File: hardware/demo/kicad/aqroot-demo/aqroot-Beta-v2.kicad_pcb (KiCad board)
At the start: 6 copper layers, 72 x 148 mm, 311 parts, among them J1 FH69-50S-0.5SH, J2 Molex_5025700893, J3 USB_C_Receptacle_USB2.0_16P, J4 JST-PH-2 BATTERY, J5 COMMUNITY_PORT_1x24, J6 JST-PH-2 SPEAKER, J7 BM02B-ACHSS-GAN-ETF, J8 QWIIC_STEMMA_QT, Q1 AO3400A, Q10 2N7002, Q2 NTMD4820N, Q3 NTMD4820N, Q4 BSS138, Q5 AO3401A, Q6 BSS138, Q7 BSS138, Q8 BSS138, Q9 BSS138, SW1 BOOT, SW2 UP, SW3 DOWN, SW4 LEFT, SW5 RIGHT, SW6 A_SELECT, SW7 B_BACK, SW9 SW_SPDT, U1 ESP32-S3-WROOM-1, U10 USBLC6-2SC6, U11 BQ25185, U12 TPS63020, U13 TPS61023, U14 MAX17048, U16 TCA4307DGKR, U17 TPS61169DCKR, U18 LTC4368-1, U19 TLV7032, U2 PCAL9535APW, U20 TPS22950C, U21 TPS61023, U22 TPS22950C, U3 PCAL9535APW, U4 BMI270, U5 MAX98357A, U6 TSOP38238, U7 E07-400M10S, U8 E22-900M22S, U9 ST25R3916-AQET, Y1 27.12MHz 10pF 3225-4P

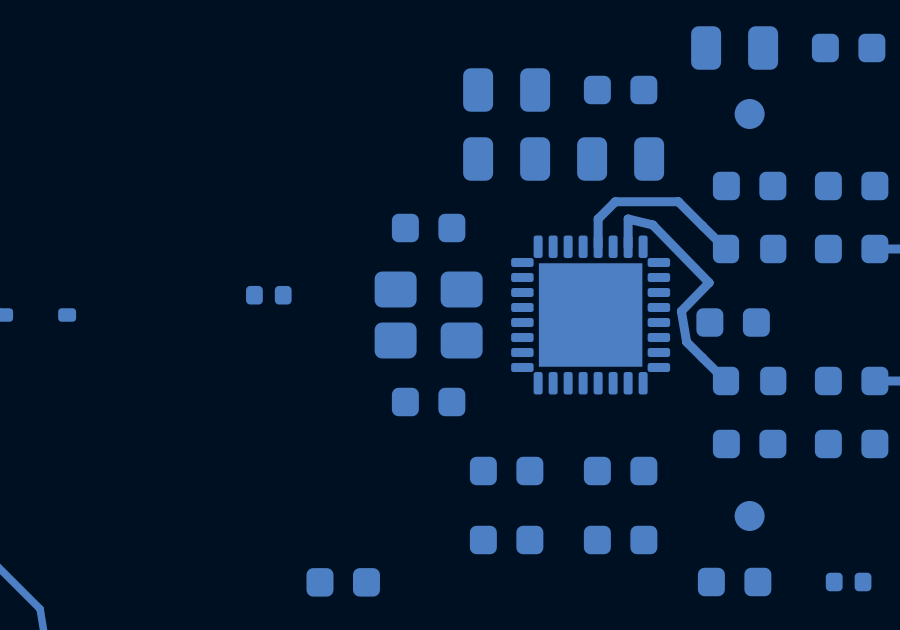
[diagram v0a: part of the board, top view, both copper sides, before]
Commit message: demo: route NFC crystal pair
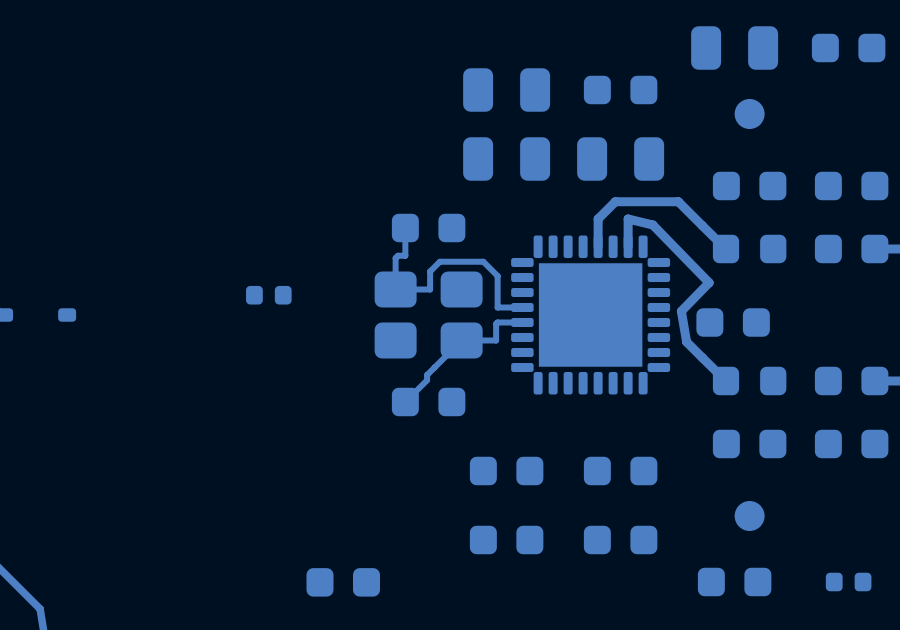
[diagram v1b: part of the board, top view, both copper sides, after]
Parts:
- moved C79 5.80 mm to (28.6, 32.9)
- moved C80 5.80 mm to (28.6, 27.1)
- turned Y1 to 180 degrees
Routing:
- net /04_SPI_B_RADIOS_NFC/NFC_XIN: track 0.00 -> 8.54 mm
- net /04_SPI_B_RADIOS_NFC/NFC_XOUT: track 0.00 -> 5.42 mm
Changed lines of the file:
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@@
 	(footprint "Capacitor_SMD:C_0603_1608Metric"
 		(layer "B.Cu")
-		(at 28.6 32.9)
+		(at 28.6 27.1)
 		(descr "Unpolarized capacitor")
 		(tags "capacitor")
@@
 	(footprint "Capacitor_SMD:C_0603_1608Metric"
 		(layer "B.Cu")
-		(at 28.6 27.1)
+		(at 28.6 32.9)
 		(descr "Unpolarized capacitor")
 		(tags "capacitor")
@@
 	(footprint "Crystal:Crystal_SMD_3225-4Pin_3.2x2.5mm"
 		(layer "B.Cu")
-		(at 28.6 30)
+		(at 28.6 30 180)
 		(descr "Four pin crystal, GND on pins 2 and 4")
 		(property "Reference" "Y1"
-			(at 0 2.45 180)
+			(at 0 2.45 0)
 			(layer "B.SilkS")
 			(hide yes)
@@
 		)
 		(property "Value" "27.12MHz 10pF 3225-4P"
-			(at 0 -2.45 180)
+			(at 0 -2.45 0)
 			(layer "B.Fab")
 			(hide yes)
@@
 		)
 		(property "Datasheet" ""
-			(at 0 0 180)
+			(at 0 0 0)
 			(layer "B.Fab")
 			(hide yes)
@@
 		)
 		(property "Description" ""
-			(at 0 0 180)
+			(at 0 0 0)
 			(layer "B.Fab")
 			(hide yes)
@@
 		)
 		(property "KiLib_Generator" "crystal_resonator_oscillator"
-			(at 0 0 180)
+			(at 0 0 0)
 			(layer "B.SilkS")
 			(hide yes)
@@
 		(duplicate_pad_numbers_are_jumpers no)
 		(fp_line
-			(start -2.06 -1.71)
-			(end 2.06 -1.71)
+			(start -2.06 1.71)
+			(end -2.06 -1.71)
 			(stroke
 				(width 0.12)
@@
 		)
 		(fp_line
-			(start -2.06 1.71)
-			(end -2.06 -1.71)
+			(start -2.06 -1.71)
+			(end 2.06 -1.71)
 			(stroke
 				(width 0.12)
@@
 		)
 		(fp_text user "${REFERENCE}"
-			(at 0 0 180)
+			(at 0 0 0)
 			(layer "B.Fab")
 			(effects
@@
 		)
 		(pad "1" smd roundrect
-			(at -1.1 -0.85)
+			(at -1.1 -0.85 180)
 			(size 1.4 1.2)
 			(layers "B.Cu" "B.Mask" "B.Paste")
@@
 		)
 		(pad "2" smd roundrect
-			(at 1.1 -0.85)
+			(at 1.1 -0.85 180)
 			(size 1.4 1.2)
 			(layers "B.Cu" "B.Mask" "B.Paste")
@@
 		)
 		(pad "3" smd roundrect
-			(at 1.1 0.85)
+			(at 1.1 0.85 180)
 			(size 1.4 1.2)
 			(layers "B.Cu" "B.Mask" "B.Paste")
@@
 		)
 		(pad "4" smd roundrect
-			(at -1.1 0.85)
+			(at -1.1 0.85 180)
 			(size 1.4 1.2)
 			(layers "B.Cu" "B.Mask" "B.Paste")
@@
 	)
 	(segment
+		(start 30.9 30.25)
+		(end 30.85 30.3)
+		(width 0.2)
+		(layer "B.Cu")
+		(net "/04_SPI_B_RADIOS_NFC/NFC_XOUT")
+	)
+	(segment
+		(start 31.725 30.25)
+		(end 30.9 30.25)
+		(width 0.2)
+		(layer "B.Cu")
+		(net "/04_SPI_B_RADIOS_NFC/NFC_XOUT")
+	)
+	(segment
+		(start 27.825 32.9)
+		(end 28.55 32.175)
+		(width 0.2)
+		(layer "B.Cu")
+		(net "/04_SPI_B_RADIOS_NFC/NFC_XOUT")
+	)
+	(segment
+		(start 28.55 32)
+		(end 28.55 32.175)
+		(width 0.2)
+		(layer "B.Cu")
+		(net "/04_SPI_B_RADIOS_NFC/NFC_XOUT")
+	)
+	(segment
+		(start 29.7 30.85)
+		(end 28.8 31.75)
+		(width 0.2)
+		(layer "B.Cu")
+		(net "/04_SPI_B_RADIOS_NFC/NFC_XOUT")
+	)
+	(segment
+		(start 28.8 31.75)
+		(end 28.55 32)
+		(width 0.2)
+		(layer "B.Cu")
+		(net "/04_SPI_B_RADIOS_NFC/NFC_XOUT")
+	)
+	(segment
+		(start 30.85 30.3)
+		(end 30.85 30.85)
+		(width 0.2)
+		(layer "B.Cu")
+		(net "/04_SPI_B_RADIOS_NFC/NFC_XOUT")
+	)
+	(segment
+		(start 29.7 30.85)
+		(end 30.85 30.85)
+		(width 0.2)
+		(layer "B.Cu")
+		(net "/04_SPI_B_RADIOS_NFC/NFC_XOUT")
+	)
+	(segment
+		(start 27.5 29.15)
+		(end 27.5 28.1)
+		(width 0.2)
+		(layer "B.Cu")
+		(net "/04_SPI_B_RADIOS_NFC/NFC_XIN")
+	)
+	(segment
+		(start 30.9 29.75)
+		(end 30.9 28.7)
+		(width 0.2)
+		(layer "B.Cu")
+		(net "/04_SPI_B_RADIOS_NFC/NFC_XIN")
+	)
+	(segment
+		(start 27.5 29.15)
+		(end 28.65 29.15)
+		(width 0.2)
+		(layer "B.Cu")
+		(net "/04_SPI_B_RADIOS_NFC/NFC_XIN")
+	)
+	(segment
+		(start 30.425 28.225)
+		(end 28.975 28.225)
+		(width 0.2)
+		(layer "B.Cu")
+		(net "/04_SPI_B_RADIOS_NFC/NFC_XIN")
+	)
+	(segment
+		(start 28.975 28.225)
+		(end 28.65 28.55)
+		(width 0.2)
+		(layer "B.Cu")
+		(net "/04_SPI_B_RADIOS_NFC/NFC_XIN")
+	)
+	(segment
+		(start 31.725 29.75)
+		(end 30.9 29.75)
+		(width 0.2)
+		(layer "B.Cu")
+		(net "/04_SPI_B_RADIOS_NFC/NFC_XIN")
+	)
+	(segment
+		(start 27.5 28.1)
+		(end 27.575 28.025)
+		(width 0.2)
+		(layer "B.Cu")
+		(net "/04_SPI_B_RADIOS_NFC/NFC_XIN")
+	)
+	(segment
+		(start 30.9 28.7)
+		(end 30.425 28.225)
+		(width 0.2)
+		(layer "B.Cu")
+		(net "/04_SPI_B_RADIOS_NFC/NFC_XIN")
+	)
+	(segment
+		(start 27.575 28.025)
+		(end 27.825 28.025)
+		(width 0.2)
+		(layer "B.Cu")
+		(net "/04_SPI_B_RADIOS_NFC/NFC_XIN")
+	)
+	(segment
+		(start 27.825 27.1)
+		(end 27.825 28.025)
+		(width 0.2)
+		(layer "B.Cu")
+		(net "/04_SPI_B_RADIOS_NFC/NFC_XIN")
+	)
+	(segment
+		(start 28.65 28.55)
+		(end 28.65 29.15)
+		(width 0.2)
+		(layer "B.Cu")
+		(net "/04_SPI_B_RADIOS_NFC/NFC_XIN")
+	)
+	(segment

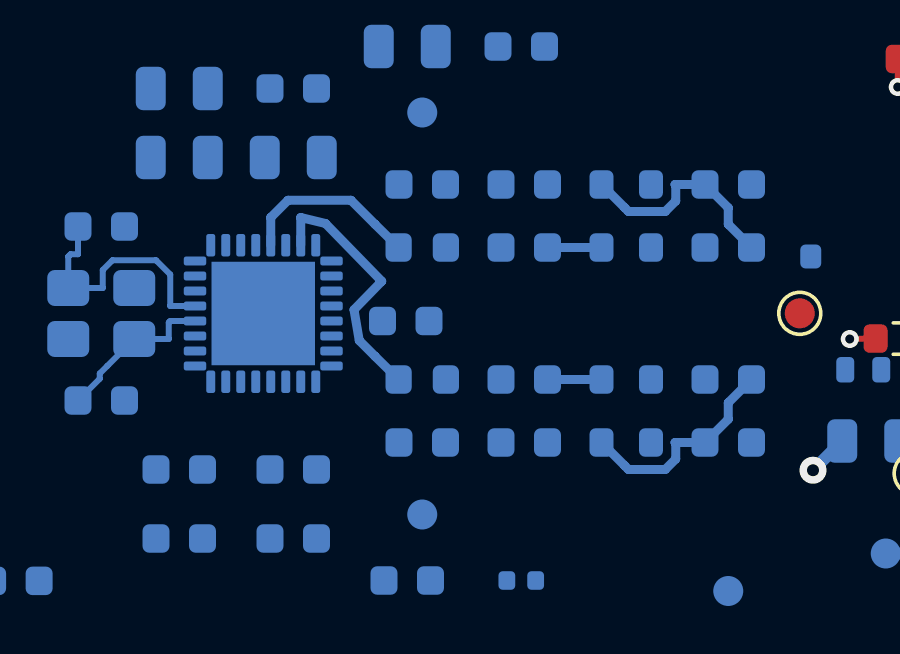
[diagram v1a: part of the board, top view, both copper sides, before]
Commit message: demo: route NFC EMC pair
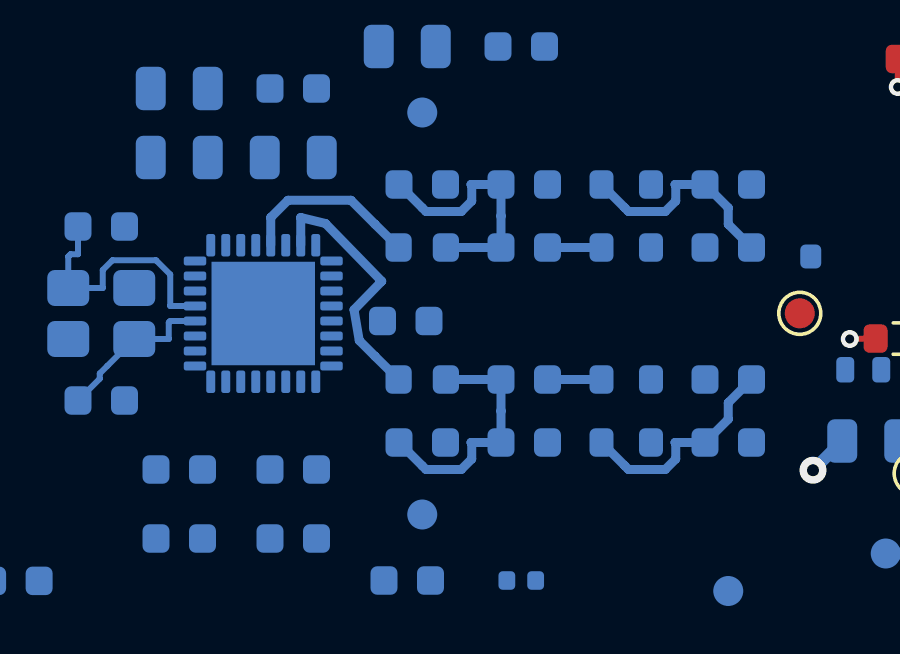
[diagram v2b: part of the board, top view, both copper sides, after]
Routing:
- net /04_SPI_B_RADIOS_NFC/NFC_EMCA: track 0.00 -> 8.76 mm
- net /04_SPI_B_RADIOS_NFC/NFC_EMCB: track 0.00 -> 8.76 mm
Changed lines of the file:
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@@
+	)
+	(segment
+		(start 40.0875 27.8)
+		(end 41.075 27.8)
+		(width 0.3)
+		(layer "B.Cu")
+		(net "/04_SPI_B_RADIOS_NFC/NFC_EMCA")
+	)
+	(segment
+		(start 41.925 27.8)
+		(end 41.925 26.775)
+		(width 0.3)
+		(layer "B.Cu")
+		(net "/04_SPI_B_RADIOS_NFC/NFC_EMCA")
+	)
+	(segment
+		(start 41.925 27.8)
+		(end 40.925 27.8)
+		(width 0.3)
+		(layer "B.Cu")
+		(net "/04_SPI_B_RADIOS_NFC/NFC_EMCA")
+	)
+	(segment
+		(start 40.95 25.7)
+		(end 40.95 26.25)
+		(width 0.3)
+		(layer "B.Cu")
+		(net "/04_SPI_B_RADIOS_NFC/NFC_EMCA")
+	)
+	(segment
+		(start 39.425 26.6)
+		(end 39.3 26.475)
+		(width 0.3)
+		(layer "B.Cu")
+		(net "/04_SPI_B_RADIOS_NFC/NFC_EMCA")
+	)
+	(segment
+		(start 40.6 26.6)
+		(end 39.425 26.6)
+		(width 0.3)
+		(layer "B.Cu")
+		(net "/04_SPI_B_RADIOS_NFC/NFC_EMCA")
+	)
+	(segment
+		(start 41.075 27.8)
+		(end 40.925 27.8)
+		(width 0.3)
+		(layer "B.Cu")
+		(net "/04_SPI_B_RADIOS_NFC/NFC_EMCA")
+	)
+	(segment
+		(start 41.925 25.7)
+		(end 40.925 25.7)
+		(width 0.3)
+		(layer "B.Cu")
+		(net "/04_SPI_B_RADIOS_NFC/NFC_EMCA")
+	)
+	(segment
+		(start 40.925 25.7)
+		(end 40.95 25.7)
+		(width 0.3)
+		(layer "B.Cu")
+		(net "/04_SPI_B_RADIOS_NFC/NFC_EMCA")
+	)
+	(segment
+		(start 41.925 26.775)
+		(end 41.925 26.725)
+		(width 0.3)
+		(layer "B.Cu")
+		(net "/04_SPI_B_RADIOS_NFC/NFC_EMCA")
+	)
+	(segment
+		(start 38.525 25.7)
+		(end 39.3 26.475)
+		(width 0.3)
+		(layer "B.Cu")
+		(net "/04_SPI_B_RADIOS_NFC/NFC_EMCA")
+	)
+	(segment
+		(start 40.95 26.25)
+		(end 40.6 26.6)
+		(width 0.3)
+		(layer "B.Cu")
+		(net "/04_SPI_B_RADIOS_NFC/NFC_EMCA")
+	)
+	(segment
+		(start 41.925 25.7)
+		(end 41.925 26.725)
+		(width 0.3)
+		(layer "B.Cu")
+		(net "/04_SPI_B_RADIOS_NFC/NFC_EMCA")
 	)
 	(segment
@@
 	)
 	(segment
+		(start 38.525 34.3)
+		(end 39.3 35.075)
+		(width 0.3)
+		(layer "B.Cu")
+		(net "/04_SPI_B_RADIOS_NFC/NFC_EMCB")
+	)
+	(segment
+		(start 41.925 34.3)
+		(end 41.925 33.275)
+		(width 0.3)
+		(layer "B.Cu")
+		(net "/04_SPI_B_RADIOS_NFC/NFC_EMCB")
+	)
+	(segment
+		(start 41.925 34.3)
+		(end 40.925 34.3)
+		(width 0.3)
+		(layer "B.Cu")
+		(net "/04_SPI_B_RADIOS_NFC/NFC_EMCB")
+	)
+	(segment
+		(start 40.0875 32.2)
+		(end 41.075 32.2)
+		(width 0.3)
+		(layer "B.Cu")
+		(net "/04_SPI_B_RADIOS_NFC/NFC_EMCB")
+	)
+	(segment
+		(start 40.6 35.2)
+		(end 39.425 35.2)
+		(width 0.3)
+		(layer "B.Cu")
+		(net "/04_SPI_B_RADIOS_NFC/NFC_EMCB")
+	)
+	(segment
+		(start 41.925 32.2)
+		(end 41.925 33.225)
+		(width 0.3)
+		(layer "B.Cu")
+		(net "/04_SPI_B_RADIOS_NFC/NFC_EMCB")
+	)
+	(segment
+		(start 40.95 34.85)
+		(end 40.6 35.2)
+		(width 0.3)
+		(layer "B.Cu")
+		(net "/04_SPI_B_RADIOS_NFC/NFC_EMCB")
+	)
+	(segment
+		(start 41.925 33.225)
+		(end 41.925 33.275)
+		(width 0.3)
+		(layer "B.Cu")
+		(net "/04_SPI_B_RADIOS_NFC/NFC_EMCB")
+	)
+	(segment
+		(start 40.95 34.3)
+		(end 40.95 34.85)
+		(width 0.3)
+		(layer "B.Cu")
+		(net "/04_SPI_B_RADIOS_NFC/NFC_EMCB")
+	)
+	(segment
+		(start 41.075 32.2)
+		(end 40.925 32.2)
+		(width 0.3)
+		(layer "B.Cu")
+		(net "/04_SPI_B_RADIOS_NFC/NFC_EMCB")
+	)
+	(segment
+		(start 39.425 35.2)
+		(end 39.3 35.075)
+		(width 0.3)
+		(layer "B.Cu")
+		(net "/04_SPI_B_RADIOS_NFC/NFC_EMCB")
+	)
+	(segment
+		(start 40.925 34.3)
+		(end 40.95 34.3)
+		(width 0.3)
+		(layer "B.Cu")
+		(net "/04_SPI_B_RADIOS_NFC/NFC_EMCB")
+	)
+	(segment
+		(start 41.925 32.2)
+		(end 40.925 32.2)
+		(width 0.3)
+		(layer "B.Cu")
+		(net "/04_SPI_B_RADIOS_NFC/NFC_EMCB")
+	)
+	(segment

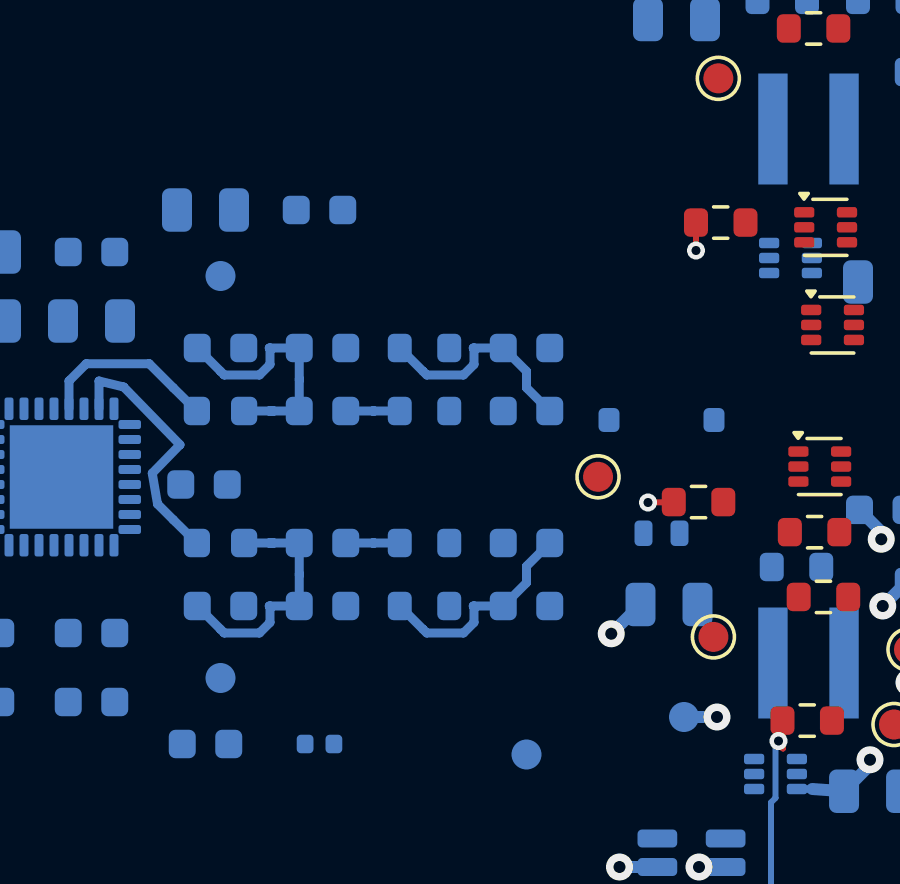
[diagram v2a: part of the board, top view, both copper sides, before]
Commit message: demo: route NFC antenna pair
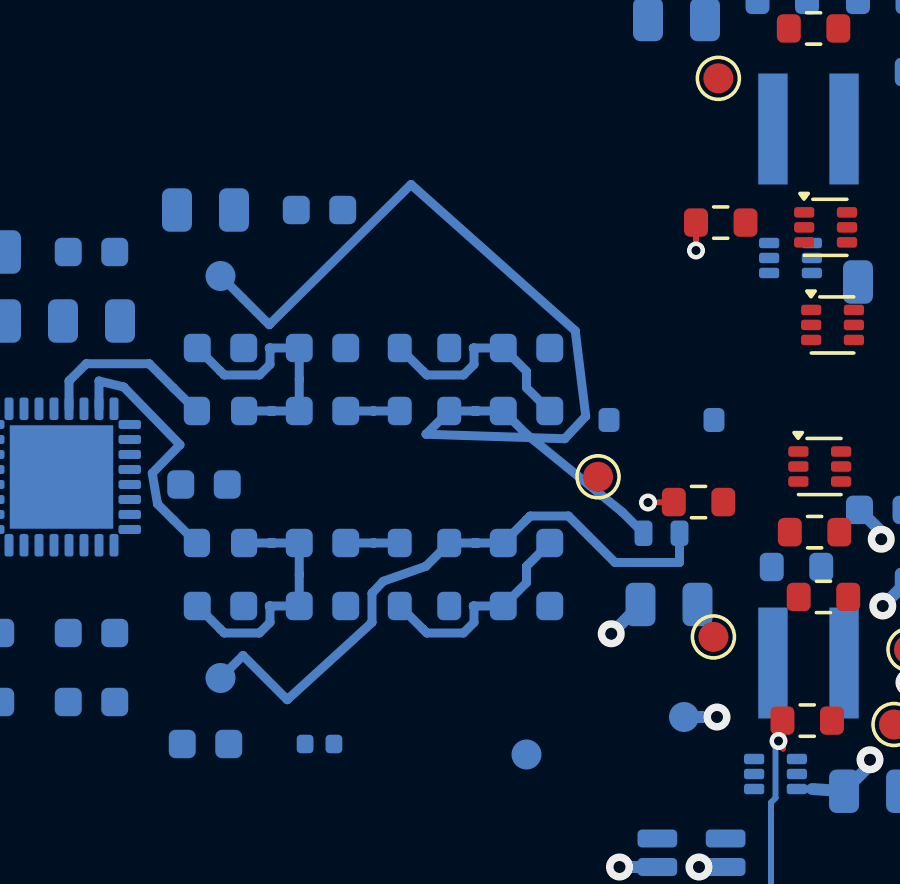
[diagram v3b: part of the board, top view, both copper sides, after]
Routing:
- net /04_SPI_B_RADIOS_NFC/NFC_ANT_A: track 0.00 -> 34.2 mm
- net /04_SPI_B_RADIOS_NFC/NFC_ANT_B: track 0.00 -> 21.1 mm
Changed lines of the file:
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@@
 	)
 	(segment
+		(start 50.9 31.3)
+		(end 52.45 32.85)
+		(width 0.3)
+		(layer "B.Cu")
+		(net "/04_SPI_B_RADIOS_NFC/NFC_ANT_B")
+	)
+	(segment
+		(start 44.35 33.875)
+		(end 44.35 34.85)
+		(width 0.3)
+		(layer "B.Cu")
+		(net "/04_SPI_B_RADIOS_NFC/NFC_ANT_B")
+	)
+	(segment
+		(start 49.625 31.3)
+		(end 50.9 31.3)
+		(width 0.3)
+		(layer "B.Cu")
+		(net "/04_SPI_B_RADIOS_NFC/NFC_ANT_B")
+	)
+	(segment
+		(start 44.725 33.475)
+		(end 44.35 33.875)
+		(width 0.3)
+		(layer "B.Cu")
+		(net "/04_SPI_B_RADIOS_NFC/NFC_ANT_B")
+	)
+	(segment
+		(start 52.45 32.85)
+		(end 54.6 32.85)
+		(width 0.3)
+		(layer "B.Cu")
+		(net "/04_SPI_B_RADIOS_NFC/NFC_ANT_B")
+	)
+	(segment
+		(start 46.15 32.975)
+		(end 44.725 33.475)
+		(width 0.3)
+		(layer "B.Cu")
+		(net "/04_SPI_B_RADIOS_NFC/NFC_ANT_B")
+	)
+	(segment
+		(start 48.725 32.2)
+		(end 47.725 32.2)
+		(width 0.3)
+		(layer "B.Cu")
+		(net "/04_SPI_B_RADIOS_NFC/NFC_ANT_B")
+	)
+	(segment
+		(start 54.6 31.875)
+		(end 54.6 32.85)
+		(width 0.3)
+		(layer "B.Cu")
+		(net "/04_SPI_B_RADIOS_NFC/NFC_ANT_B")
+	)
+	(segment
+		(start 48.725 32.2)
+		(end 49.5 31.425)
+		(width 0.3)
+		(layer "B.Cu")
+		(net "/04_SPI_B_RADIOS_NFC/NFC_ANT_B")
+	)
+	(segment
+		(start 39.3 36.7)
+		(end 40.05 35.95)
+		(width 0.3)
+		(layer "B.Cu")
+		(net "/04_SPI_B_RADIOS_NFC/NFC_ANT_B")
+	)
+	(segment
+		(start 49.5 31.425)
+		(end 49.625 31.3)
+		(width 0.3)
+		(layer "B.Cu")
+		(net "/04_SPI_B_RADIOS_NFC/NFC_ANT_B")
+	)
+	(segment
+		(start 46.925 32.2)
+		(end 47.875 32.2)
+		(width 0.3)
+		(layer "B.Cu")
+		(net "/04_SPI_B_RADIOS_NFC/NFC_ANT_B")
+	)
+	(segment
+		(start 41.525 37.425)
+		(end 40.05 35.95)
+		(width 0.3)
+		(layer "B.Cu")
+		(net "/04_SPI_B_RADIOS_NFC/NFC_ANT_B")
+	)
+	(segment
+		(start 47.875 32.2)
+		(end 47.725 32.2)
+		(width 0.3)
+		(layer "B.Cu")
+		(net "/04_SPI_B_RADIOS_NFC/NFC_ANT_B")
+	)
+	(segment
+		(start 46.925 32.2)
+		(end 46.15 32.975)
+		(width 0.3)
+		(layer "B.Cu")
+		(net "/04_SPI_B_RADIOS_NFC/NFC_ANT_B")
+	)
+	(segment
+		(start 44.35 34.85)
+		(end 41.525 37.425)
+		(width 0.3)
+		(layer "B.Cu")
+		(net "/04_SPI_B_RADIOS_NFC/NFC_ANT_B")
+	)
+	(segment
 		(start 7.95 20.05)
 		(end 7.95 11.5)
@@
 	)
 	(segment
+		(start 49.5 28.575)
+		(end 52.7 31.175)
+		(width 0.3)
+		(layer "B.Cu")
+		(net "/04_SPI_B_RADIOS_NFC/NFC_ANT_A")
+	)
+	(segment
+		(start 47.875 27.8)
+		(end 47.725 27.8)
+		(width 0.3)
+		(layer "B.Cu")
+		(net "/04_SPI_B_RADIOS_NFC/NFC_ANT_A")
+	)
+	(segment
+		(start 51.475 27.975)
+		(end 51.125 25.125)
+		(width 0.3)
+		(layer "B.Cu")
+		(net "/04_SPI_B_RADIOS_NFC/NFC_ANT_A")
+	)
+	(segment
+		(start 40.925 24.925)
+		(end 40.05 24.05)
+		(width 0.3)
+		(layer "B.Cu")
+		(net "/04_SPI_B_RADIOS_NFC/NFC_ANT_A")
+	)
+	(segment
+		(start 51.125 25.125)
+		(end 45.65 20.25)
+		(width 0.3)
+		(layer "B.Cu")
+		(net "/04_SPI_B_RADIOS_NFC/NFC_ANT_A")
+	)
+	(segment
+		(start 46.925 27.8)
+		(end 46.15 28.575)
+		(width 0.3)
+		(layer "B.Cu")
+		(net "/04_SPI_B_RADIOS_NFC/NFC_ANT_A")
+	)
+	(segment
+		(start 53.4 31.875)
+		(end 52.7 31.175)
+		(width 0.3)
+		(layer "B.Cu")
+		(net "/04_SPI_B_RADIOS_NFC/NFC_ANT_A")
+	)
+	(segment
+		(start 48.725 27.8)
+		(end 47.725 27.8)
+		(width 0.3)
+		(layer "B.Cu")
+		(net "/04_SPI_B_RADIOS_NFC/NFC_ANT_A")
+	)
+	(segment
+		(start 39.3 23.3)
+		(end 40.05 24.05)
+		(width 0.3)
+		(layer "B.Cu")
+		(net "/04_SPI_B_RADIOS_NFC/NFC_ANT_A")
+	)
+	(segment
+		(start 46.15 28.575)
+		(end 50.775 28.725)
+		(width 0.3)
+		(layer "B.Cu")
+		(net "/04_SPI_B_RADIOS_NFC/NFC_ANT_A")
+	)
+	(segment
+		(start 46.925 27.8)
+		(end 47.875 27.8)
+		(width 0.3)
+		(layer "B.Cu")
+		(net "/04_SPI_B_RADIOS_NFC/NFC_ANT_A")
+	)
+	(segment
+		(start 45.65 20.25)
+		(end 40.925 24.925)
+		(width 0.3)
+		(layer "B.Cu")
+		(net "/04_SPI_B_RADIOS_NFC/NFC_ANT_A")
+	)
+	(segment
+		(start 48.725 27.8)
+		(end 49.5 28.575)
+		(width 0.3)
+		(layer "B.Cu")
+		(net "/04_SPI_B_RADIOS_NFC/NFC_ANT_A")
+	)
+	(segment
+		(start 50.775 28.725)
+		(end 51.475 27.975)
+		(width 0.3)
+		(layer "B.Cu")
+		(net "/04_SPI_B_RADIOS_NFC/NFC_ANT_A")
+	)
+	(segment

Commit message: demo: route fuel gauge alert
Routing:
- net /01_POWER_TREE/MAX17048_ALRT_N: track 0.00 -> 4.31 mm, vias 0 -> 2
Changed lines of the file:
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@@
 		(net "/01_POWER_TREE/BAT_PROT_SHDN_CTL")
+	)
+	(via
+		(at 2.675 81.225)
+		(size 0.6)
+		(drill 0.3)
+		(layers "F.Cu" "B.Cu")
+		(net "/01_POWER_TREE/MAX17048_ALRT_N")
+	)
+	(via
+		(at 5.25 81.2)
+		(size 0.6)
+		(drill 0.3)
+		(layers "F.Cu" "B.Cu")
+		(net "/01_POWER_TREE/MAX17048_ALRT_N")
+	)
+	(segment
+		(start 3.225 81.765)
+		(end 2.675 81.225)
+		(width 0.2)
+		(layer "B.Cu")
+		(net "/01_POWER_TREE/MAX17048_ALRT_N")
+	)
+	(segment
+		(start 5.25 80.25)
+		(end 5.25 81.2)
+		(width 0.2)
+		(layer "B.Cu")
+		(net "/01_POWER_TREE/MAX17048_ALRT_N")
+	)
+	(segment
+		(start 2.7 81.2)
+		(end 2.675 81.225)
+		(width 0.2)
+		(layer "In3.Cu")
+		(net "/01_POWER_TREE/MAX17048_ALRT_N")
+	)
+	(segment
+		(start 5.25 81.2)
+		(end 2.7 81.2)
+		(width 0.2)
+		(layer "In3.Cu")
+		(net "/01_POWER_TREE/MAX17048_ALRT_N")
 	)
 	(segment
